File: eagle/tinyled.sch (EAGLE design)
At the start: 11 parts, among them IC1 ATtiny85

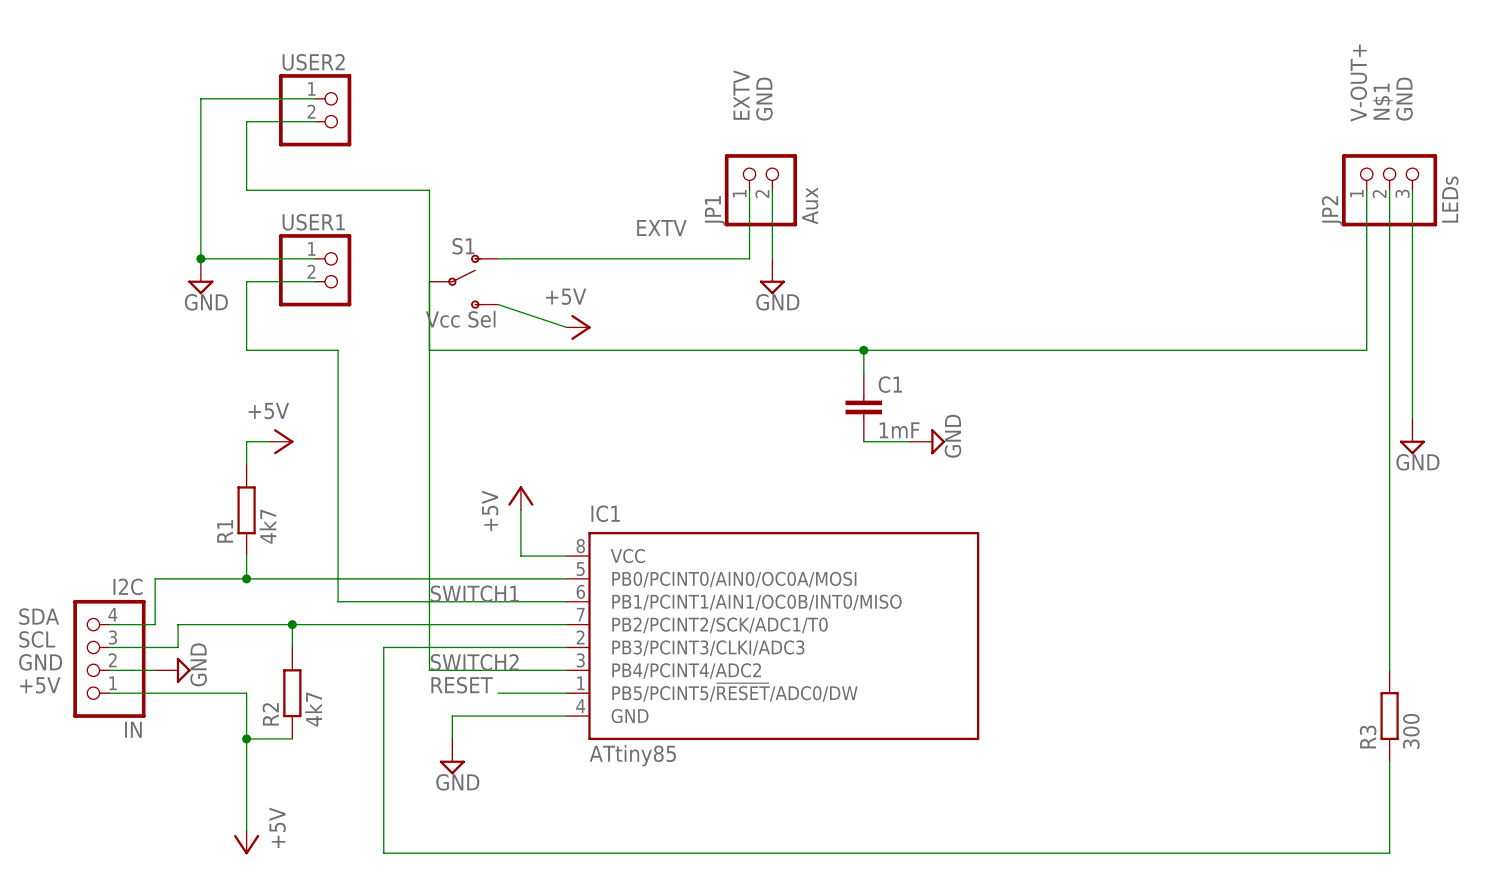
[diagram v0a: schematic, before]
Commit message: fixed shiort circuits in design
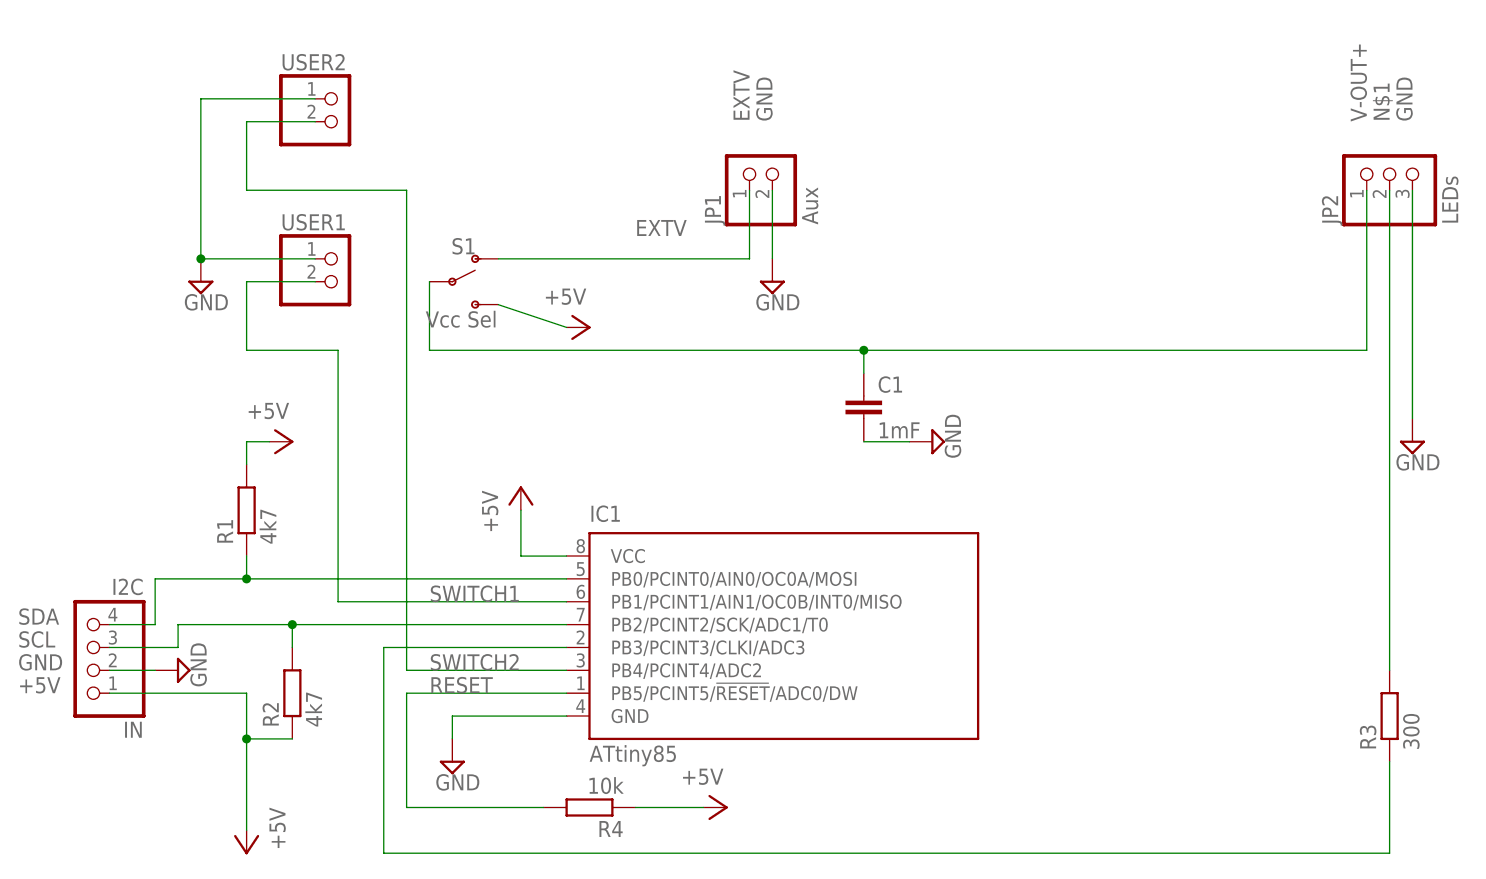
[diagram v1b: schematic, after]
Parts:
- added R4: 10k, eagle-ltspice:R0204/7
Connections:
- net +5V: now also R4.1
- net RESET: now also R4.2
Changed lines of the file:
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@@
 <part name="USER2" library="pinhead" library_urn="urn:adsk.eagle:library:325" deviceset="PINHD-1X2" device="" package3d_urn="urn:adsk.eagle:package:22435/2"/>
 <part name="SUPPLY6" library="supply2" library_urn="urn:adsk.eagle:library:372" deviceset="GND" device=""/>
+<part name="R4" library="eagle-ltspice" library_urn="urn:adsk.eagle:library:217" deviceset="R" device="0204/7" package3d_urn="urn:adsk.eagle:package:13274/1" value="10k"/>
+<part name="P+4" library="supply1" library_urn="urn:adsk.eagle:library:371" deviceset="+5V" device=""/>
 </parts>
 <sheets>
@@
 <instance part="USER2" gate="G$1" x="15.24" y="78.74"/>
 <instance part="SUPPLY6" gate="GND" x="0" y="60.96"/>
+<instance part="R4" gate="G$1" x="43.18" y="2.54" rot="R180"/>
+<instance part="P+4" gate="1" x="58.42" y="2.54" rot="R270"/>
 </instances>
 <busses>
@@
 <label x="-20.32" y="15.24" size="1.778" layer="95"/>
 </segment>
+<segment>
+<pinref part="R4" gate="G$1" pin="1"/>
+<pinref part="P+4" gate="1" pin="+5V"/>
+<wire x1="48.26" y1="2.54" x2="55.88" y2="2.54" width="0.1524" layer="91"/>
+</segment>
 </net>
 <net name="SDA" class="0">
@@
 <segment>
 <pinref part="IC1" gate="G$1" pin="PB5/PCINT5/!RESET!/ADC0/DW"/>
-<wire x1="40.64" y1="15.24" x2="33.02" y2="15.24" width="0.1524" layer="91"/>
 <label x="25.4" y="15.24" size="1.778" layer="95"/>
+<pinref part="R4" gate="G$1" pin="2"/>
+<wire x1="38.1" y1="2.54" x2="22.86" y2="2.54" width="0.1524" layer="91"/>
+<wire x1="22.86" y1="2.54" x2="22.86" y2="15.24" width="0.1524" layer="91"/>
+<wire x1="22.86" y1="15.24" x2="40.64" y2="15.24" width="0.1524" layer="91"/>
 </segment>
 </net>
@@
 <wire x1="12.7" y1="78.74" x2="5.08" y2="78.74" width="0.1524" layer="91"/>
 <wire x1="5.08" y1="78.74" x2="5.08" y2="71.12" width="0.1524" layer="91"/>
-<wire x1="5.08" y1="71.12" x2="25.4" y2="71.12" width="0.1524" layer="91"/>
-<wire x1="25.4" y1="71.12" x2="25.4" y2="17.78" width="0.1524" layer="91"/>
+<wire x1="5.08" y1="71.12" x2="22.86" y2="71.12" width="0.1524" layer="91"/>
+<wire x1="22.86" y1="71.12" x2="22.86" y2="17.78" width="0.1524" layer="91"/>
 <pinref part="IC1" gate="G$1" pin="PB4/PCINT4/ADC2"/>
-<wire x1="25.4" y1="17.78" x2="40.64" y2="17.78" width="0.1524" layer="91"/>
+<wire x1="22.86" y1="17.78" x2="40.64" y2="17.78" width="0.1524" layer="91"/>
 <label x="25.4" y="17.78" size="1.778" layer="95"/>
 </segment>
@@
 </sheet>
 </sheets>
+<errors>
+</errors>
 </schematic>
 </drawing>
